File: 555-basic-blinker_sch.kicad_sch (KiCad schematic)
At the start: 8 parts, among them U1 ICM7555xP

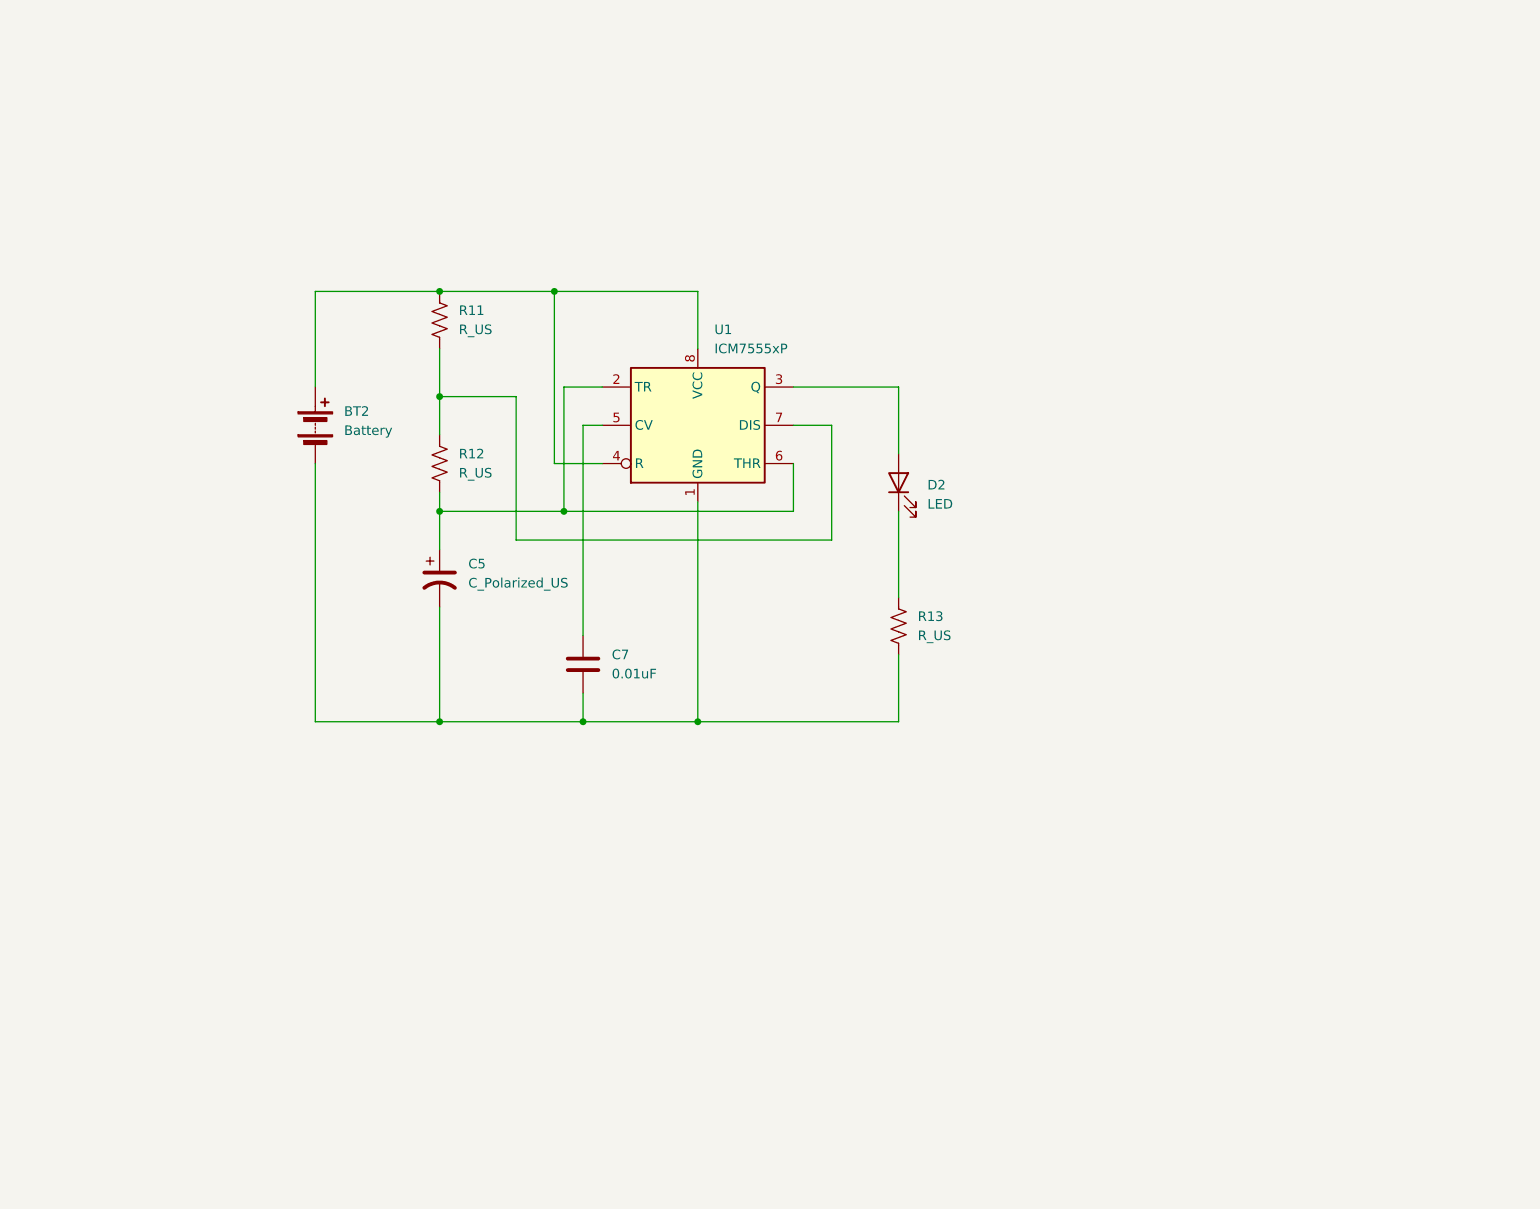
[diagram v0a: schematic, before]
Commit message: added the 3 main 555 configurations
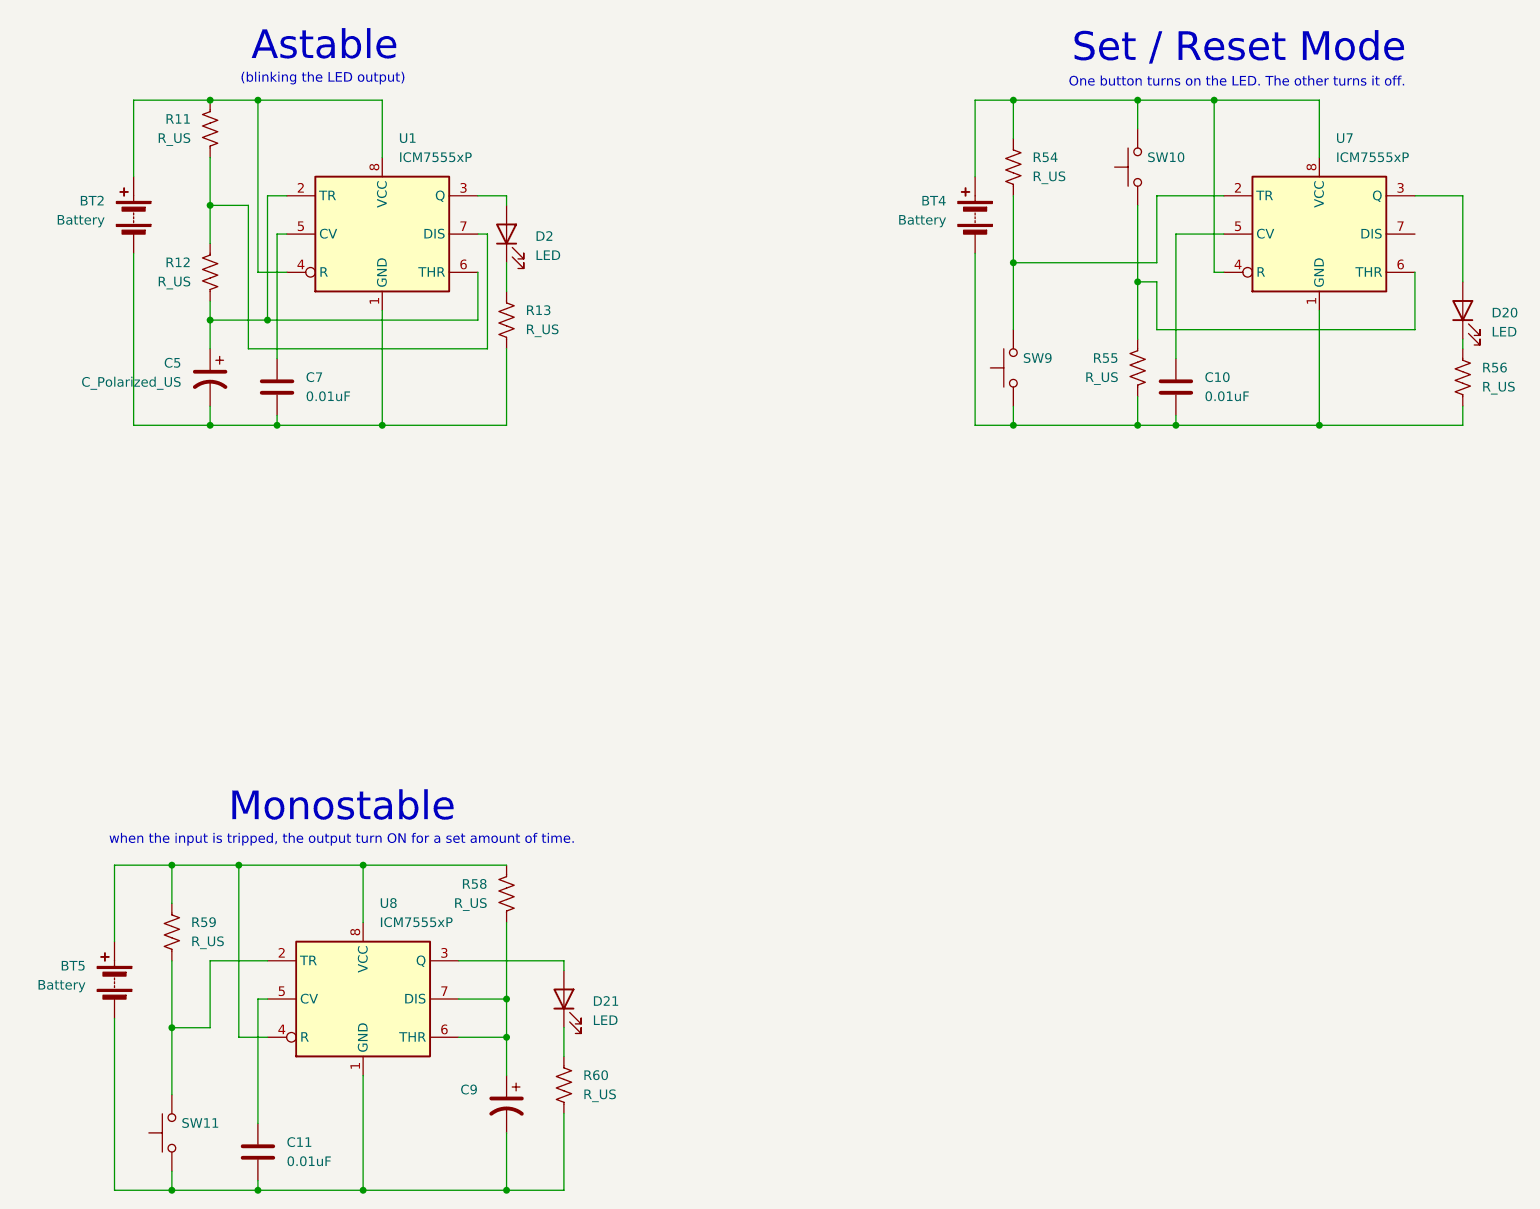
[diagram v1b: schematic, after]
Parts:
- added BT4, BT5: Battery, symbol Device:Battery
- added C10, C11: 0.01uF, symbol Device:C
- added C9: C_Polarized_US, symbol Device:C_Polarized_US
- added D20, D21: LED, symbol Device:LED
- added R54, R55, R56, R58, R59, R60: R_US, symbol Device:R_US
- added SW10, SW11, SW9: SW_Push, symbol Switch:SW_Push
- added U7, U8: ICM7555xP, Package_DIP:DIP-8_W7.62mm, symbol Timer:ICM7555xP
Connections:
- new net: C11.1, U8.5 (CV)
- new net: BT5.2 (-), C11.2, C9.2, R60.2, SW11.1, U8.1 (GND)
- new net: C9.1, R58.2, U8.6 (THR), U8.7 (DIS)
- new net: C10.1, U7.5 (CV)
- new net: BT4.2 (-), C10.2, R55.2, R56.2, SW9.1, U7.1 (GND)
- new net: R55.1, SW10.1, U7.6 (THR)
- new net: BT4.1 (+), R54.1, SW10.2, U7.4 (R), U7.8 (VCC)
- new net: D20.1 (K), R56.1
- new net: BT5.1 (+), R58.1, R59.1, U8.4 (R), U8.8 (VCC)
- new net: R59.2, SW11.2, U8.2 (TR)
- new net: D21.2 (A), U8.3 (Q)
- new net: D21.1 (K), R60.1
- new net: R54.2, SW9.2, U7.2 (TR)
- new net: D20.2 (A), U7.3 (Q)
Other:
- note added: "(blinking the LED output)"
- note added: "Astable"
- note added: "Monostable"
- note added: "One button turns on the LED. The other turns it off."
- note added: "Set / Reset Mode"
- note added: "when the input is tripped, the output turn ON for a set amount of time."
- title: 555 Basic Blinker -> 555 timer - the 3 common modes
- moved on the sheet: BT2, C5, C7, D2, R11, R12, R13, U1
